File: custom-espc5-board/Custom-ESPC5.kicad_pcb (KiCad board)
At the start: 2 copper layers, 42 parts, among them J1 Screw_Terminal_01x02, J10 Barrel_Jack, J12 Conn_01x05, J13 Conn_01x05, J2 Conn_01x03, J3 Conn_01x03, J4 USB_C_Receptacle_USB2.0_14P, J5 Conn_01x03, J6 Screw_Terminal_01x03, SW1 SW_Nidec_CAS-120A1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

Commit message: closed kicad
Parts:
- moved C3 95.3 mm to (274.0, 115.4)
- moved C4 95.3 mm to (274.0, 117.4)
- moved J2 95.3 mm to (226.7, 76.7)
- moved J3 95.3 mm to (238.6, 76.7)
- moved C14 93.2 mm to (144.1, 45.1), turned to 90 degrees
- moved R3 92.4 mm to (203.1, 53.6)
- moved R4 92.4 mm to (203.1, 55.6)
- moved R5 86.2 mm to (181.0, 49.0), turned to 90 degrees
- moved C9 85.5 mm to (142.4, 52.3), turned to -90 degrees
- moved C6 83.5 mm to (184.0, 44.3), turned to 90 degrees
- moved D2 81.9 mm to (214.2, 58.5)
- moved R7 81.7 mm to (176.8, 44.5), turned to -90 degrees
- moved C5 81.4 mm to (182.0, 44.3), turned to 90 degrees
- moved R15 79.6 mm to (149.5, 45.3), turned to 90 degrees
- moved J5 76.1 mm to (84.7, 111.0)
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
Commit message: aa
fitting things into board dimensions
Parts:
- added REF**: MountingHole_4.5mm, MountingHole:MountingHole_4.5mm, F.Cu at (111.0, 95.0)
- added REF**: MountingHole_4.5mm, MountingHole:MountingHole_4.5mm, F.Cu at (111.0, 160.0)
- added REF**: MountingHole_4.5mm, MountingHole:MountingHole_4.5mm, F.Cu at (46.0, 95.0)
- added REF**: MountingHole_4.5mm, MountingHole:MountingHole_4.5mm, F.Cu at (46.0, 161.0)
- moved C4 200.3 mm to (74.1, 104.1), turned to -90 degrees
- moved C3 200.0 mm to (74.2, 106.6), turned to -90 degrees
- moved J3 196.5 mm to (50.9, 134.4), turned to -90 degrees
- moved J2 181.7 mm to (50.9, 122.5), turned to -90 degrees
- moved D2 127.0 mm to (101.4, 116.8), turned to 90 degrees
- moved J1 116.6 mm to (96.2, 153.0), turned to 180 degrees
- moved R4 114.9 mm to (106.0, 117.0), turned to -90 degrees
- moved R3 114.3 mm to (108.0, 117.0), turned to -90 degrees
- moved R8 100.6 mm to (89.5, 144.5)
- moved R9 100.6 mm to (85.9, 144.5)
- moved U5 100.0 mm to (95.0, 138.1)
- moved J6 99.0 mm to (77.0, 150.0)
- moved R17 99.0 mm to (61.4, 150.4)
- moved SW1 99.0 mm to (65.4, 158.3)
- moved U9 99.0 mm to (65.6, 149.6)
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
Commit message: board layout
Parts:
- removed REF** (x4): MountingHole_4.5mm, MountingHole:MountingHole_4.5mm
- removed U10: CP2102N-Axx-xQFN28, Package_DFN_QFN:QFN-28-1EP_5x5mm_P0.5mm_EP3.35x3.35mm
- added D3: D, Diode_SMD:USC-TOS, F.Cu at (89.2, 112.2)
- added U3: CP2102N-Axx-xQFN24, Package_DFN_QFN:QFN-24-1EP_4x4mm_P0.5mm_EP2.6x2.6mm, F.Cu at (93.0, 118.2)
- R1: value 910 -> 430
- R2: value 270 -> 240
- moved U9 112.4 mm to (173.0, 116.7)
- moved SW1 109.7 mm to (167.3, 117.9)
- moved U12 105.5 mm to (161.0, 110.3), turned to 0 degrees
- moved SW3 99.5 mm to (167.8, 123.8)
- moved JP2 96.3 mm to (172.8, 108.4), turned to 0 degrees
- moved C14 94.2 mm to (154.7, 120.9), turned to 0 degrees
- moved R17 92.8 mm to (148.8, 119.5), turned to 0 degrees
- moved JP1 90.7 mm to (168.3, 108.4), turned to 0 degrees
- moved R18 86.2 mm to (148.8, 121.5), turned to 0 degrees
- moved J1 84.7 mm to (163.1, 101.0), turned to 0 degrees
- moved J6 84.3 mm to (145.6, 101.0), turned to 0 degrees
- moved R15 82.9 mm to (145.9, 125.5), turned to 0 degrees
- moved C4 81.0 mm to (154.7, 113.0), turned to 0 degrees
- moved C3 80.6 mm to (154.7, 111.0), turned to 0 degrees
- moved R16 74.9 mm to (148.8, 117.6), turned to 0 degrees
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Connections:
- C5 pad 1: Net-(U10-VREGIN) -> Net-(U12-IN)
- C6 pad 1: Net-(U10-VREGIN) -> Net-(U12-IN)
- C9 pad 1: +3.3V -> Net-(D3-A)
- D1 pad 1: +5V -> +3.3V
- D2 pad 2: Net-(U10-VREGIN) -> Net-(U12-IN)
- J4 pad A4: Net-(U10-VREGIN) -> Net-(U12-IN)
- J4 pad A9: Net-(U10-VREGIN) -> Net-(U12-IN)
- J4 pad B4: Net-(U10-VREGIN) -> Net-(U12-IN)
- J4 pad B9: Net-(U10-VREGIN) -> Net-(U12-IN)
- R5 pad 1: Net-(U10-VREGIN) -> Net-(U12-IN)
- U12 pad 1: +3.3V -> Net-(D3-A)
- U12 pad 3: +5V -> Net-(U12-IN)
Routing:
- net Net-(D1-A): track 0.00 -> 13.9 mm
- net Net-(U2-VI): track 0.00 -> 9.51 mm
- net GND: track 0.00 -> 4.98 mm, vias 0 -> 2
- net Net-(U2-ADJ): track 0.00 -> 4.60 mm
- added copper zone on In1.Cu, net GND
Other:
- board outline added: 67.6 x 80 mm
- copper layers 2 -> 4

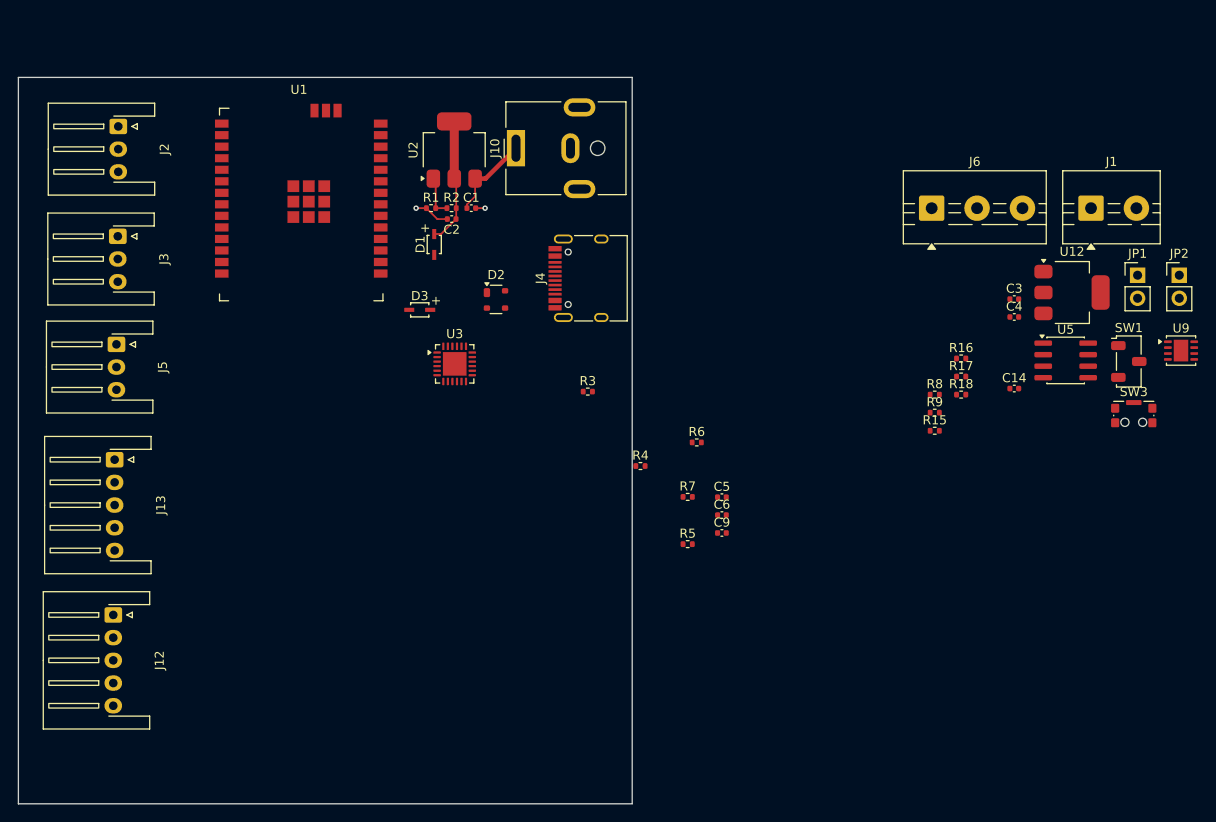
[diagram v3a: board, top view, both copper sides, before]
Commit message: Finish preliminary board tracings (NOT COMPLETE)
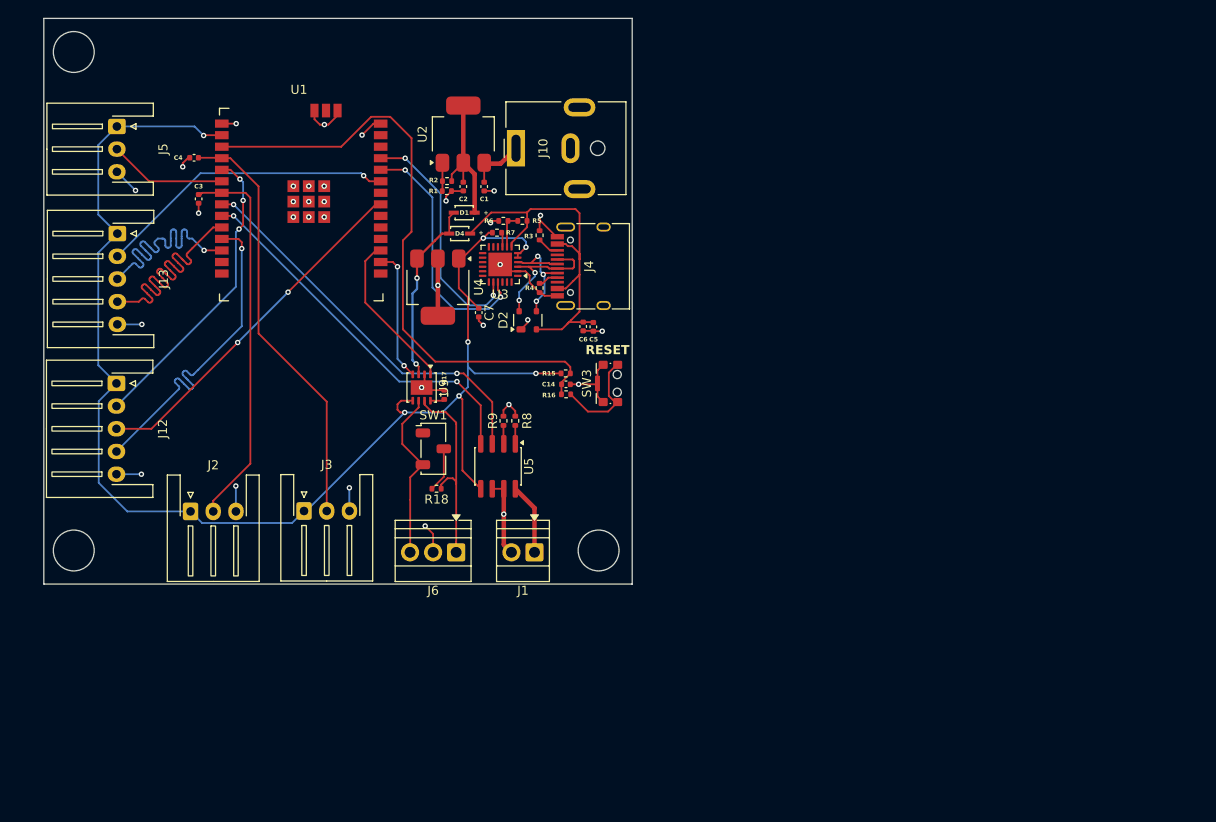
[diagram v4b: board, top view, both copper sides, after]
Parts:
- removed C9: 47uF, Capacitor_SMD:C_0402_1005Metric
- removed D3: D, Diode_SMD:USC-TOS
- removed JP1, JP2: Jumper_2_Open, Connector_PinHeader_2.54mm:PinHeader_1x02_P2.54mm_Vertical
- removed U12: LM3940, Package_TO_SOT_SMD:SOT-223-3_TabPin2
- added ?: , , F.Cu at (51.1, 138.7)
- added ?: , , F.Cu at (108.9, 138.7)
- added ?: , , F.Cu at (51.1, 83.8)
- added C7: 47uF, Capacitor_SMD:C_0402_1005Metric, F.Cu at (95.7, 112.5)
- added D4: D, Diode_SMD:USC-TOS, F.Cu at (93.6, 103.8)
- added U4: LM3940, Package_TO_SOT_SMD:SOT-223-3_TabPin2, F.Cu at (91.2, 109.7)
- J1: footprint TerminalBlock:TerminalBlock_MaiXu_MX126-5.0-02P_1x02_P5.00mm -> TerminalBlock:TerminalBlock_Xinya_XY308-2.54-2P_1x02_P2.54mm_Horizontal
- J6: footprint TerminalBlock:TerminalBlock_MaiXu_MX126-5.0-03P_1x03_P5.00mm -> TerminalBlock:TerminalBlock_Xinya_XY308-2.54-3P_1x03_P2.54mm_Horizontal
- R1: value 430 -> 910
- moved C4 92.0 mm to (64.3, 95.5), turned to 180 degrees
- moved C3 90.5 mm to (64.8, 100.0), turned to -90 degrees
- moved U9 83.7 mm to (89.4, 120.8), turned to -90 degrees
- moved SW1 77.2 mm to (90.7, 127.5)
- moved J1 72.1 mm to (101.8, 138.9), turned to 180 degrees
- moved J6 64.6 mm to (93.2, 138.9), turned to 180 degrees
- moved U5 63.6 mm to (97.8, 129.4), turned to -90 degrees
- moved R18 58.7 mm to (91.0, 131.9), turned to 180 degrees
- moved SW3 57.7 mm to (110.2, 120.3), turned to 90 degrees
- moved R17 57.0 mm to (91.9, 121.6), turned to 90 degrees
- moved C14 49.4 mm to (105.3, 120.4), turned to 180 degrees
- moved R9 47.5 mm to (98.4, 124.4), turned to 90 degrees
- moved R8 46.3 mm to (99.7, 124.4), turned to 90 degrees
- moved R16 43.7 mm to (105.3, 121.5)
- moved J2 43.1 mm to (64.0, 134.4), turned to 0 degrees
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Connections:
- D1 pad 1: +3.3V -> +5V
- U1 pad 24: unconnected-(U1-U0RXD/GPIO12-Pad24) -> /UART RX
- U1 pad 25: unconnected-(U1-U0TXD/GPIO11-Pad25) -> /UART TX
- U3 pad 20: /UART RX -> /UART TX
- U3 pad 21: /UART TX -> /UART RX
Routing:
- net +3.3V: track 0.00 -> 157.7 mm, vias 0 -> 7
- net GND: track 4.98 -> 80.5 mm, vias 2 -> 33
- net /CHIP_PU: track 0.00 -> 68.3 mm
- net /SIG2: track 0.00 -> 46.8 mm
- net Net-(D4-A): track 0.00 -> 43.8 mm
- net /I2C SDA: track 0.00 -> 43.4 mm, vias 0 -> 2
- net /SIG1: track 0.00 -> 42.2 mm
- net /I2C SCL: track 0.00 -> 41.9 mm, vias 0 -> 2
- net /A2: track 0.00 -> 39.7 mm, vias 0 -> 2
- net /IDX2: track 0.00 -> 36.2 mm, vias 0 -> 1
- net /IDX1: track 0.00 -> 34.2 mm
- net /B2: track 0.00 -> 33.8 mm, vias 0 -> 3
- net /B1: track 0.00 -> 33.2 mm, vias 0 -> 1
- net /A1: track 0.00 -> 29.4 mm, vias 0 -> 1
- net /UART RX: track 0.00 -> 27.7 mm, vias 0 -> 2
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- added copper zone on In2.Cu, net GND
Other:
- board size 67.6 x 80 mm -> 64.8 x 62.3 mm
- board text added: "RESET"
